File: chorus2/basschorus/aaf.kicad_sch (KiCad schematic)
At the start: 7 parts, among them U8 TL072

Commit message: code implementation
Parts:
- removed U8: TL072, kicad-legacy/Housings_DIP.pretty:DIP-8_W7.62mm, symbol Amplifier_Operational:TL072
- added U4: TL074, symbol Amplifier_Operational:TL074
- renumbered R11 to R18, R12 to R19, R17 to R20
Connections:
- net OUT: now also U4.1, U4.2 (-)
- net at C17.2, R20.1: now also U4.3 (+)
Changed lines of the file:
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@@
-	)
-	(symbol
-		(lib_id "Amplifier_Operational:TL072")
-		(at 175.26 100.33 0)
-		(unit 1)
-		(exclude_from_sim no)
-		(in_bom yes)
-		(on_board yes)
-		(dnp no)
-		(property "Reference" "U8"
-			(at 175.26 91.0082 0)
-			(effects
-				(font
-					(size 1.27 1.27)
-				)
-			)
-		)
-		(property "Value" "TL072"
-			(at 175.26 93.3196 0)
-			(effects
-				(font
-					(size 1.27 1.27)
-				)
-			)
-		)
-		(property "Footprint" "kicad-legacy/Housings_DIP.pretty:DIP-8_W7.62mm"
-			(at 175.26 100.33 0)
-			(effects
-				(font
-					(size 1.27 1.27)
-				)
-				(hide yes)
-			)
-		)
-		(property "Datasheet" "http://www.ti.com/lit/ds/symlink/tl071.pdf"
-			(at 175.26 100.33 0)
-			(effects
-				(font
-					(size 1.27 1.27)
-				)
-				(hide yes)
-			)
-		)
-		(property "Description" ""
-			(at 175.26 100.33 0)
-			(effects
-				(font
-					(size 1.27 1.27)
-				)
-			)
-		)
-		(pin "1"
-		)
-		(pin "2"
-		)
-		(pin "3"
-		)
-		(pin "5"
-		)
-		(pin "6"
-		)
-		(pin "7"
-		)
-		(pin "4"
-		)
-		(pin "8"
-		)
-		(instances
-			(project "basschorus"
-				(path "/7f3b4bac-3b2a-4af0-92ae-ccc3fcedc393/55ec0f37-0f57-44d5-88f5-fd537ba2da80"
-					(reference "U8")
-					(unit 1)
-				)
-			)
-		)
 	)
 	(symbol
@@
 		(on_board yes)
 		(dnp no)
-		(property "Reference" "R11"
+		(property "Reference" "R18"
 			(at 127 92.5322 90)
 			(effects
@@
 			(project "basschorus"
 				(path "/7f3b4bac-3b2a-4af0-92ae-ccc3fcedc393/55ec0f37-0f57-44d5-88f5-fd537ba2da80"
-					(reference "R11")
+					(reference "R18")
 					(unit 1)
 				)
@@
 		(on_board yes)
 		(dnp no)
-		(property "Reference" "R17"
+		(property "Reference" "R20"
 			(at 153.67 92.5322 90)
 			(effects
@@
 			(project "basschorus"
 				(path "/7f3b4bac-3b2a-4af0-92ae-ccc3fcedc393/55ec0f37-0f57-44d5-88f5-fd537ba2da80"
-					(reference "R17")
+					(reference "R20")
 					(unit 1)
 				)
@@
 		(on_board yes)
 		(dnp no)
-		(property "Reference" "R12"
+		(property "Reference" "R19"
 			(at 139.7 92.5322 90)
 			(effects
@@
 			(project "basschorus"
 				(path "/7f3b4bac-3b2a-4af0-92ae-ccc3fcedc393/55ec0f37-0f57-44d5-88f5-fd537ba2da80"
-					(reference "R12")
+					(reference "R19")
 					(unit 1)
 				)
@@
 					(unit 1)
 				)
+			)
+		)
+	)
+	(symbol
+		(lib_id "Amplifier_Operational:TL074")
+		(at 175.26 100.33 0)
+		(unit 1)
+		(exclude_from_sim no)
+		(in_bom yes)
+		(on_board yes)
+		(dnp no)
+		(fields_autoplaced yes)
+		(property "Reference" "U4"
+			(at 175.26 90.17 0)
+			(effects
+				(font
+					(size 1.27 1.27)
+				)
+			)
+		)
+		(property "Value" "TL074"
+			(at 175.26 92.71 0)
+			(effects
+				(font
+					(size 1.27 1.27)
+				)
+			)
+		)
+		(property "Footprint" ""
+			(at 173.99 97.79 0)
+			(effects
+				(font
+					(size 1.27 1.27)
+				)
+				(hide yes)
+			)
+		)
+		(property "Datasheet" "http://www.ti.com/lit/ds/symlink/tl071.pdf"
+			(at 176.53 95.25 0)
+			(effects
+				(font
+					(size 1.27 1.27)
+				)
+				(hide yes)
+			)
+		)
+		(property "Description" "Quad Low-Noise JFET-Input Operational Amplifiers, DIP-14/SOIC-14"
+			(at 175.26 100.33 0)
+			(effects
+				(font
+					(size 1.27 1.27)
+				)
+				(hide yes)
+			)
+		)
+		(pin "1"
+		)
+		(pin "5"
+		)
+		(pin "3"
+		)
+		(pin "2"
+		)
+		(pin "6"
+		)
+		(pin "7"
+		)
+		(pin "10"
+		)
+		(pin "9"
+		)
+		(pin "8"
+		)
+		(pin "12"
+		)
+		(pin "13"
+		)
+		(pin "4"
+		)
+		(pin "11"
+		)
+		(pin "14"
+		)
+		(instances
+			(project ""
+				(path "/7f3b4bac-3b2a-4af0-92ae-ccc3fcedc393/55ec0f37-0f57-44d5-88f5-fd537ba2da80"
+					(reference "U4")
+					(unit 1)
+				)

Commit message: update filters
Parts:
- added R35: 43k, kicad-legacy/kicad-footprints/Resistor_THT.pretty:R_Axial_DIN0204_L3.6mm_D1.6mm_P2.54mm_Vertical, symbol Device:R
- added R36: 56k, kicad-legacy/kicad-footprints/Resistor_THT.pretty:R_Axial_DIN0204_L3.6mm_D1.6mm_P2.54mm_Vertical, symbol Device:R
- added R37: 100k, kicad-legacy/kicad-footprints/Resistor_THT.pretty:R_Axial_DIN0204_L3.6mm_D1.6mm_P2.54mm_Vertical, symbol Device:R
- added RV5: R_TRIM_10K, kicad-legacy/Potentiometers.pretty:Potentiometer_Trimmer_Bourns_3296W, symbol Device:R_Potentiometer_Trim
- added TP1: TestPoint, symbol Connector:TestPoint
- C16: value 470n -> 150n
- C17: value 33n -> 6.8n
- C18: value 220n -> 470p
- R19: renamed from R18; value 100k -> 910
- R20: renamed from R19; value 820k -> 43k
- R21: renamed from R20; value 330k -> 110k
- renumbered U4 to U2
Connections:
- net GND: now also R37.2
- net OUT: now also R35.1; no longer U2.2 (-)
- net at R21.1, U2.3 (+): now also C18.2; no longer C17.2
- net at R20.1, R21.2: now also C17.2, R35.2; no longer C18.2
- new net: R36.2, RV5.3
- new net: R37.1, RV5.1
- new net: RV5.2, TP1.1, U2.2 (-)
- new net +5V: R36.1
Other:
- note added: "3.2V reference. adjustable range 3.3 to 3.0"
- note added: "3rd order multiple-feedback LPF with 3.2V DC offset and DC gain K of -1 NOTE=could apply a DC gain to scale input to proper 120mV level Assuming input is already 120mV_rms (-14dBu), the total bandwidth of the BDD is 50dB so we need at least 50db of rejection at 1/2 the lowest clock frequency (5kHz). Note that some rejection is already happining with the bandpass of the previous stage. http://sim.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"
- note removed: "3rd order sallen key LPF Butterworth, Cutoff = 3.5KHz http://sim.okawa-denshi.jp/en/Sallen3tool.php"
- moved on the sheet: C17, C18

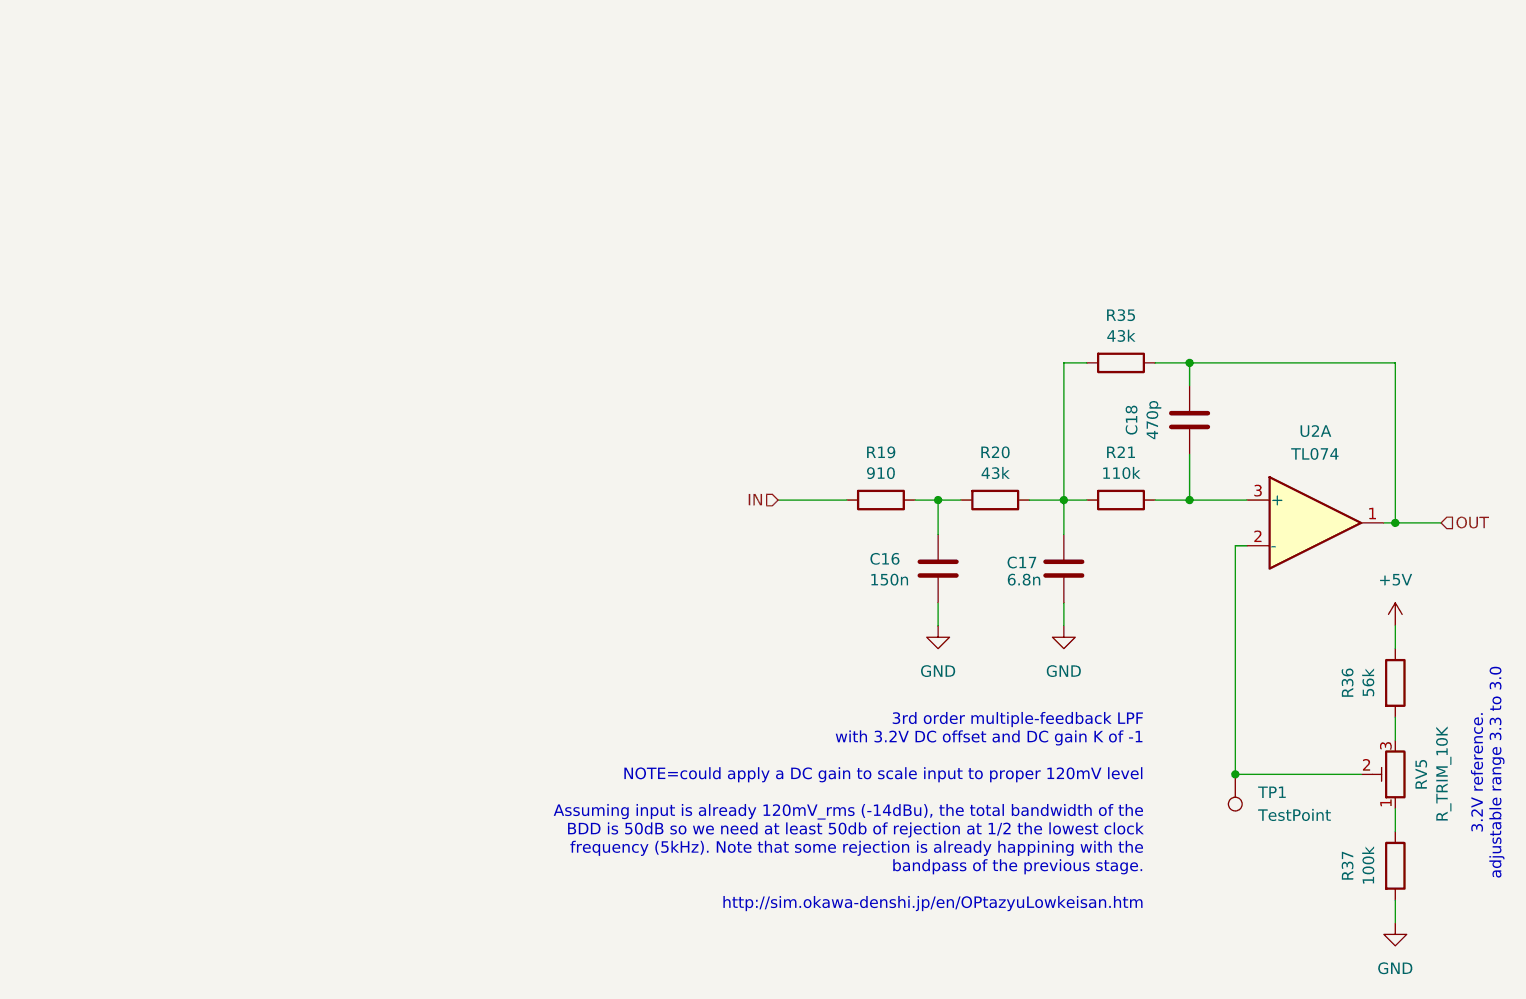
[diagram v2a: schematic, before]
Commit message: update designs based on new calculations
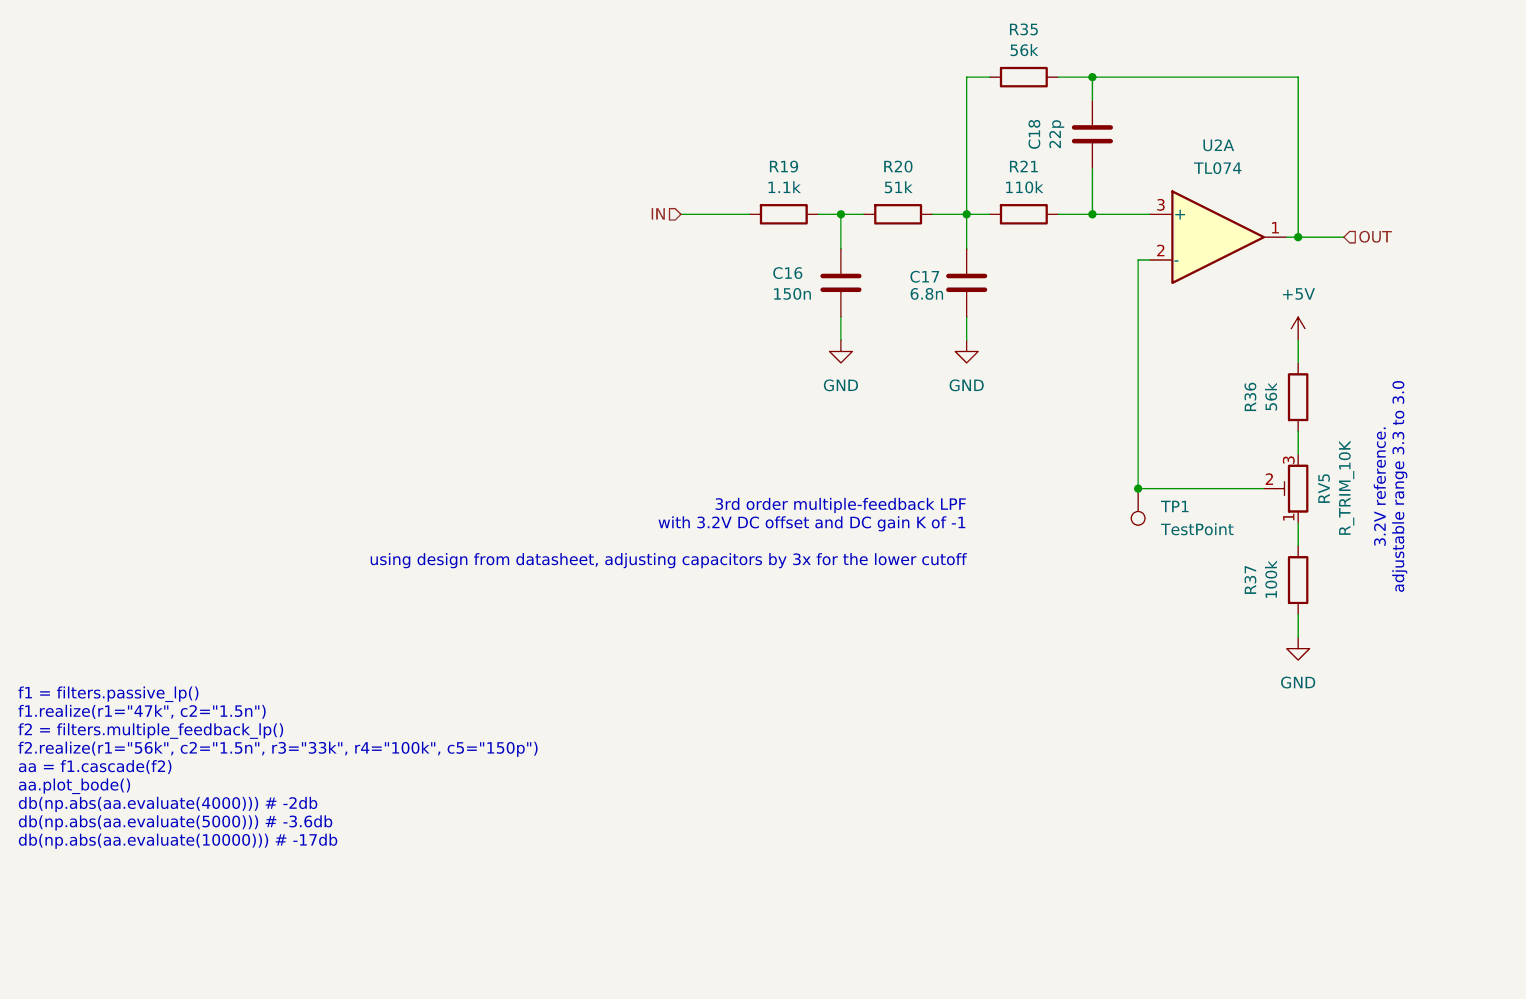
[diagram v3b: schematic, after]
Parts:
- C18: value 470p -> 22p
- R19: value 910 -> 1.1k
- R20: value 43k -> 51k
- R35: value 43k -> 56k
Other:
- note added: "3rd order multiple-feedback LPF with 3.2V DC offset and DC gain K of -1 using design from datasheet, adjusting capacitors by 3x for the lower cutoff"
- note added: "f1 = filters.passive_lp() f1.realize(r1="47k", c2="1.5n") f2 = filters.multiple_feedback_lp() f2.realize(r1="56k", c2="1.5n", r3="33k", r4="100k", c5="150p") aa = f1.cascade(f2) aa.plot_bode() db(np.abs(aa.evaluate(4000))) # -2db db(np.abs(aa.evaluate(5000))) # -3.6db db(np.abs(aa.evaluate(10000))) # -17db"
- note removed: "3rd order multiple-feedback LPF with 3.2V DC offset and DC gain K of -1 NOTE=could apply a DC gain to scale input to proper 120mV level Assuming input is already 120mV_rms (-14dBu), the total bandwidth of the BDD is 50dB so we need at least 50db of rejection at 1/2 the lowest clock frequency (5kHz). Note that some rejection is already happining with the bandpass of the previous stage. http://sim.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"
- moved on the sheet: C16, C17, C18, R19, R20, R21, R35, R36, R37, RV5, TP1

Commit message: assign parts for testing
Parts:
- C21: renamed from C16; footprint (none) -> Capacitor_THT:C_Rect_L7.0mm_W2.5mm_P5.00mm
- C22: renamed from C17; footprint (none) -> Capacitor_THT:C_Rect_L7.0mm_W2.5mm_P5.00mm
- C23: renamed from C18; footprint (none) -> Capacitor_THT:C_Rect_L7.0mm_W2.5mm_P5.00mm
- R22: renamed from R19; footprint kicad-legacy/kicad-footprints/Resistor_THT.pretty:R_Axial_DIN0204_L3.6mm_D1.6mm_P2.54mm_Vertical -> Resistor_THT:R_Axial_DIN0204_L3.6mm_D1.6mm_P5.08mm_Horizontal
- R23: renamed from R20; footprint kicad-legacy/kicad-footprints/Resistor_THT.pretty:R_Axial_DIN0204_L3.6mm_D1.6mm_P2.54mm_Vertical -> Resistor_THT:R_Axial_DIN0204_L3.6mm_D1.6mm_P5.08mm_Horizontal
- R24: renamed from R35; footprint kicad-legacy/kicad-footprints/Resistor_THT.pretty:R_Axial_DIN0204_L3.6mm_D1.6mm_P2.54mm_Vertical -> Resistor_THT:R_Axial_DIN0204_L3.6mm_D1.6mm_P5.08mm_Horizontal
- R25: renamed from R21; footprint kicad-legacy/kicad-footprints/Resistor_THT.pretty:R_Axial_DIN0204_L3.6mm_D1.6mm_P2.54mm_Vertical -> Resistor_THT:R_Axial_DIN0204_L3.6mm_D1.6mm_P5.08mm_Horizontal
- R26: renamed from R36; footprint kicad-legacy/kicad-footprints/Resistor_THT.pretty:R_Axial_DIN0204_L3.6mm_D1.6mm_P2.54mm_Vertical -> Resistor_THT:R_Axial_DIN0204_L3.6mm_D1.6mm_P5.08mm_Horizontal
- R27: renamed from R37; footprint kicad-legacy/kicad-footprints/Resistor_THT.pretty:R_Axial_DIN0204_L3.6mm_D1.6mm_P2.54mm_Vertical -> Resistor_THT:R_Axial_DIN0204_L3.6mm_D1.6mm_P5.08mm_Horizontal
- RV6: renamed from RV5; footprint kicad-legacy/Potentiometers.pretty:Potentiometer_Trimmer_Bourns_3296W -> Potentiometer_THT:Potentiometer_Vishay_T73YP_Vertical
- TP1: footprint (none) -> TestPoint:TestPoint_THTPad_2.5x2.5mm_Drill1.2mm
- U2: footprint (none) -> Package_SO:SO-14_3.9x8.65mm_P1.27mm
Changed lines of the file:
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@@
 			)
 		)
-		(property "Footprint" ""
+		(property "Footprint" "Package_SO:SO-14_3.9x8.65mm_P1.27mm"
 			(at 163.195 66.04 0)
 			(effects
@@
 		(on_board yes)
 		(dnp no)
-		(property "Reference" "R36"
+		(property "Reference" "R26"
 			(at 168.0972 86.36 90)
 			(effects
@@
 			)
 		)
-		(property "Footprint" "kicad-legacy/kicad-footprints/Resistor_THT.pretty:R_Axial_DIN0204_L3.6mm_D1.6mm_P2.54mm_Vertical"
+		(property "Footprint" "Resistor_THT:R_Axial_DIN0204_L3.6mm_D1.6mm_P5.08mm_Horizontal"
 			(at 171.577 86.36 90)
 			(effects
@@
 			(project "basschorus"
 				(path "/7f3b4bac-3b2a-4af0-92ae-ccc3fcedc393/55ec0f37-0f57-44d5-88f5-fd537ba2da80"
-					(reference "R36")
+					(reference "R26")
 					(unit 1)
 				)
@@
 		(on_board yes)
 		(dnp no)
-		(property "Reference" "R19"
+		(property "Reference" "R22"
 			(at 116.205 60.7822 90)
 			(effects
@@
 			)
 		)
-		(property "Footprint" "kicad-legacy/kicad-footprints/Resistor_THT.pretty:R_Axial_DIN0204_L3.6mm_D1.6mm_P2.54mm_Vertical"
+		(property "Footprint" "Resistor_THT:R_Axial_DIN0204_L3.6mm_D1.6mm_P5.08mm_Horizontal"
 			(at 116.205 64.262 90)
 			(effects
@@
 			(project "basschorus"
 				(path "/7f3b4bac-3b2a-4af0-92ae-ccc3fcedc393/55ec0f37-0f57-44d5-88f5-fd537ba2da80"
-					(reference "R19")
+					(reference "R22")
 					(unit 1)
 				)
@@
 		(on_board yes)
 		(dnp no)
-		(property "Reference" "R35"
+		(property "Reference" "R24"
 			(at 142.875 45.5422 90)
 			(effects
@@
 			)
 		)
-		(property "Footprint" "kicad-legacy/kicad-footprints/Resistor_THT.pretty:R_Axial_DIN0204_L3.6mm_D1.6mm_P2.54mm_Vertical"
+		(property "Footprint" "Resistor_THT:R_Axial_DIN0204_L3.6mm_D1.6mm_P5.08mm_Horizontal"
 			(at 142.875 49.022 90)
 			(effects
@@
 			(project "basschorus"
 				(path "/7f3b4bac-3b2a-4af0-92ae-ccc3fcedc393/55ec0f37-0f57-44d5-88f5-fd537ba2da80"
-					(reference "R35")
+					(reference "R24")
 					(unit 1)
 				)
@@
 		(on_board yes)
 		(dnp no)
-		(property "Reference" "C17"
+		(property "Reference" "C22"
 			(at 130.175 73.025 0)
 			(effects
@@
 			)
 		)
-		(property "Footprint" ""
+		(property "Footprint" "Capacitor_THT:C_Rect_L7.0mm_W2.5mm_P5.00mm"
 			(at 135.5598 69.85 0)
 			(effects
@@
 			(project "basschorus"
 				(path "/7f3b4bac-3b2a-4af0-92ae-ccc3fcedc393/55ec0f37-0f57-44d5-88f5-fd537ba2da80"
-					(reference "C17")
+					(reference "C22")
 					(unit 1)
 				)
@@
 		(on_board yes)
 		(dnp no)
-		(property "Reference" "RV5"
+		(property "Reference" "RV6"
 			(at 176.276 96.52 90)
 			(effects
@@
 			)
 		)
-		(property "Footprint" "kicad-legacy/Potentiometers.pretty:Potentiometer_Trimmer_Bourns_3296W"
+		(property "Footprint" "Potentiometer_THT:Potentiometer_Vishay_T73YP_Vertical"
 			(at 173.355 96.52 0)
 			(effects
@@
 			(project "basschorus"
 				(path "/7f3b4bac-3b2a-4af0-92ae-ccc3fcedc393/55ec0f37-0f57-44d5-88f5-fd537ba2da80"
-					(reference "RV5")
+					(reference "RV6")
 					(unit 1)
 				)
@@
 		(on_board yes)
 		(dnp no)
-		(property "Reference" "R21"
+		(property "Reference" "R25"
 			(at 142.875 60.7822 90)
 			(effects
@@
 			)
 		)
-		(property "Footprint" "kicad-legacy/kicad-footprints/Resistor_THT.pretty:R_Axial_DIN0204_L3.6mm_D1.6mm_P2.54mm_Vertical"
+		(property "Footprint" "Resistor_THT:R_Axial_DIN0204_L3.6mm_D1.6mm_P5.08mm_Horizontal"
 			(at 142.875 64.262 90)
 			(effects
@@
 			(project "basschorus"
 				(path "/7f3b4bac-3b2a-4af0-92ae-ccc3fcedc393/55ec0f37-0f57-44d5-88f5-fd537ba2da80"
-					(reference "R21")
+					(reference "R25")
 					(unit 1)
 				)
@@
 		(on_board yes)
 		(dnp no)
-		(property "Reference" "R20"
+		(property "Reference" "R23"
 			(at 128.905 60.7822 90)
 			(effects
@@
 			)
 		)
-		(property "Footprint" "kicad-legacy/kicad-footprints/Resistor_THT.pretty:R_Axial_DIN0204_L3.6mm_D1.6mm_P2.54mm_Vertical"
+		(property "Footprint" "Resistor_THT:R_Axial_DIN0204_L3.6mm_D1.6mm_P5.08mm_Horizontal"
 			(at 128.905 64.262 90)
 			(effects
@@
 			(project "basschorus"
 				(path "/7f3b4bac-3b2a-4af0-92ae-ccc3fcedc393/55ec0f37-0f57-44d5-88f5-fd537ba2da80"
-					(reference "R20")
+					(reference "R23")
 					(unit 1)
 				)
@@
 		(on_board yes)
 		(dnp no)
-		(property "Reference" "C18"
+		(property "Reference" "C23"
 			(at 144.0942 57.15 90)
 			(effects
@@
 			)
 		)
-		(property "Footprint" ""
+		(property "Footprint" "Capacitor_THT:C_Rect_L7.0mm_W2.5mm_P5.00mm"
 			(at 151.4602 60.96 0)
 			(effects
@@
 			(project "basschorus"
 				(path "/7f3b4bac-3b2a-4af0-92ae-ccc3fcedc393/55ec0f37-0f57-44d5-88f5-fd537ba2da80"
-					(reference "C18")
+					(reference "C23")
 					(unit 1)
 				)
@@
 		(on_board yes)
 		(dnp no)
-		(property "Reference" "C16"
+		(property "Reference" "C21"
 			(at 114.935 72.6186 0)
 			(effects
@@
 			)
 		)
-		(property "Footprint" ""
+		(property "Footprint" "Capacitor_THT:C_Rect_L7.0mm_W2.5mm_P5.00mm"
 			(at 121.5898 69.85 0)
 			(effects
@@
 			(project "basschorus"
 				(path "/7f3b4bac-3b2a-4af0-92ae-ccc3fcedc393/55ec0f37-0f57-44d5-88f5-fd537ba2da80"
-					(reference "C16")
+					(reference "C21")
 					(unit 1)
 				)
@@
 			)
 		)
-		(property "Footprint" ""
+		(property "Footprint" "TestPoint:TestPoint_THTPad_2.5x2.5mm_Drill1.2mm"
 			(at 150.495 96.52 0)
 			(effects
@@
 		(dnp no)
 		(fields_autoplaced yes)
-		(property "Reference" "#PWR049"
+		(property "Reference" "#PWR059"
 			(at 122.555 86.36 0)
 			(effects
@@
 			(project "basschorus"
 				(path "/7f3b4bac-3b2a-4af0-92ae-ccc3fcedc393/55ec0f37-0f57-44d5-88f5-fd537ba2da80"
-					(reference "#PWR049")
+					(reference "#PWR059")
 					(unit 1)
 				)
@@
 		(on_board yes)
 		(dnp no)
-		(property "Reference" "R37"
+		(property "Reference" "R27"
 			(at 168.0972 106.68 90)
 			(effects
@@
 			)
 		)
-		(property "Footprint" "kicad-legacy/kicad-footprints/Resistor_THT.pretty:R_Axial_DIN0204_L3.6mm_D1.6mm_P2.54mm_Vertical"
+		(property "Footprint" "Resistor_THT:R_Axial_DIN0204_L3.6mm_D1.6mm_P5.08mm_Horizontal"
 			(at 171.577 106.68 90)
 			(effects
@@
 			(project "basschorus"
 				(path "/7f3b4bac-3b2a-4af0-92ae-ccc3fcedc393/55ec0f37-0f57-44d5-88f5-fd537ba2da80"
-					(reference "R37")
+					(reference "R27")
 					(unit 1)
 				)
@@
 		(dnp no)
 		(fields_autoplaced yes)
-		(property "Reference" "#PWR050"
+		(property "Reference" "#PWR060"
 			(at 136.525 86.36 0)
 			(effects
@@
 			(project "basschorus"
 				(path "/7f3b4bac-3b2a-4af0-92ae-ccc3fcedc393/55ec0f37-0f57-44d5-88f5-fd537ba2da80"
-					(reference "#PWR050")
+					(reference "#PWR060")
 					(unit 1)
 				)
@@
 		(dnp no)
 		(fields_autoplaced yes)
-		(property "Reference" "#PWR058"
+		(property "Reference" "#PWR062"
 			(at 173.355 119.38 0)
 			(effects
@@
 			(project "basschorus"
 				(path "/7f3b4bac-3b2a-4af0-92ae-ccc3fcedc393/55ec0f37-0f57-44d5-88f5-fd537ba2da80"
-					(reference "#PWR058")
+					(reference "#PWR062")
 					(unit 1)
 				)
@@
 		(dnp no)
 		(fields_autoplaced yes)
-		(property "Reference" "#PWR057"
+		(property "Reference" "#PWR061"
 			(at 173.355 83.82 0)
 			(effects
@@
 			(project ""
 				(path "/7f3b4bac-3b2a-4af0-92ae-ccc3fcedc393/55ec0f37-0f57-44d5-88f5-fd537ba2da80"
-					(reference "#PWR057")
-					(unit 1)
-				)
+					(reference "#PWR061")
+					(unit 1)
+				)

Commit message: started layout
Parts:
- TP1: value TestPoint -> DC
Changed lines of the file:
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@@
 		(fields_autoplaced yes)
 		(property "Reference" "TP1"
-			(at 158.115 98.5519 0)
+			(at 157.48 98.5519 0)
 			(effects
 				(font
@@
 			)
 		)
-		(property "Value" "TestPoint"
-			(at 158.115 101.0919 0)
+		(property "Value" "DC"
+			(at 157.48 101.0919 0)
 			(effects
 				(font

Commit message: basic layout
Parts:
- removed U2: TL074, Package_SO:SO-14_3.9x8.65mm_P1.27mm, symbol Amplifier_Operational:TL074
- added U2: TL074, Package_SO:SO-14_3.9x8.65mm_P1.27mm, symbol Amplifier_Operational:TL074
- R22, R23, R24, R25, R26, R27: footprint Resistor_THT:R_Axial_DIN0204_L3.6mm_D1.6mm_P5.08mm_Horizontal -> Resistor_THT:R_Axial_DIN0204_L3.6mm_D1.6mm_P2.54mm_Vertical
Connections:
- net OUT: now also U2.14
- net at RV6.2, TP1.1: now also U2.12 (+)
- net at C23.2, R25.1: now also U2.13 (-)
